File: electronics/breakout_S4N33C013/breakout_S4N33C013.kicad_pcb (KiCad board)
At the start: 4 copper layers, 2 parts

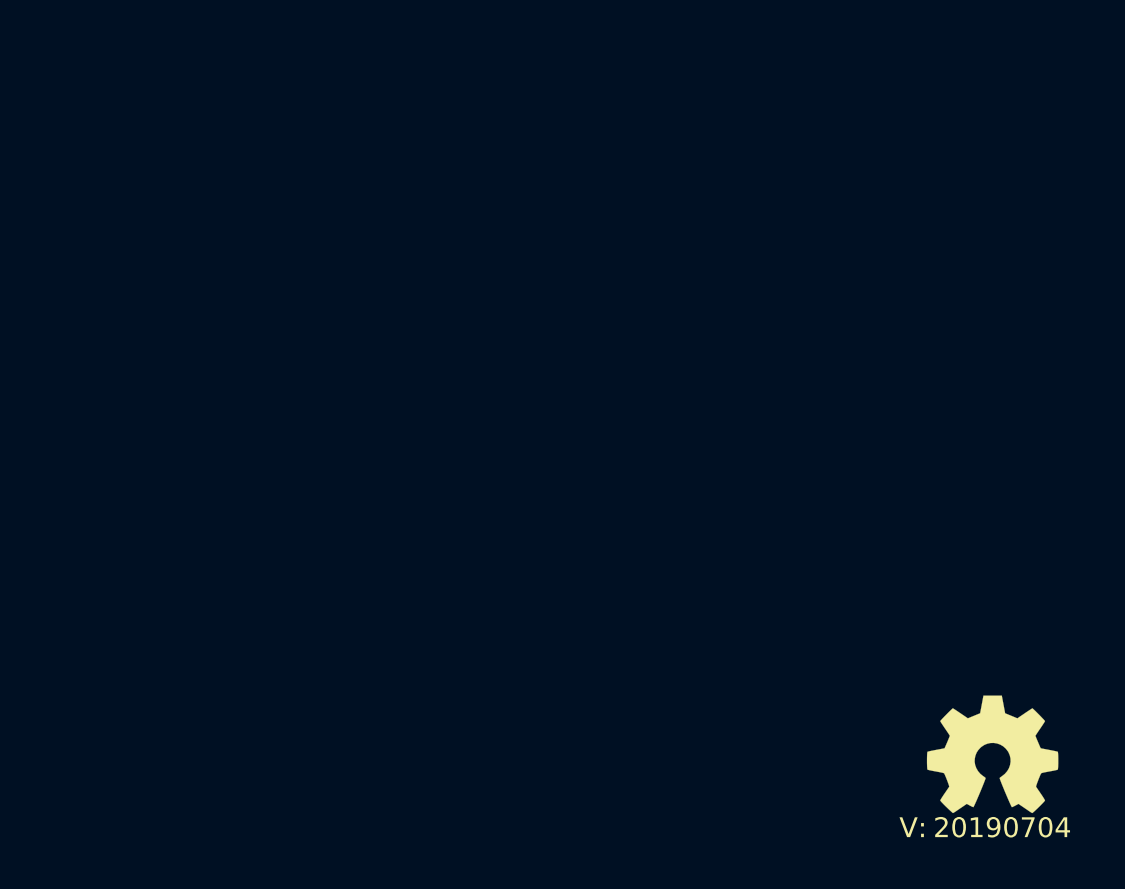
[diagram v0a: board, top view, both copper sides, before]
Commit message: Started initial layout for breakout
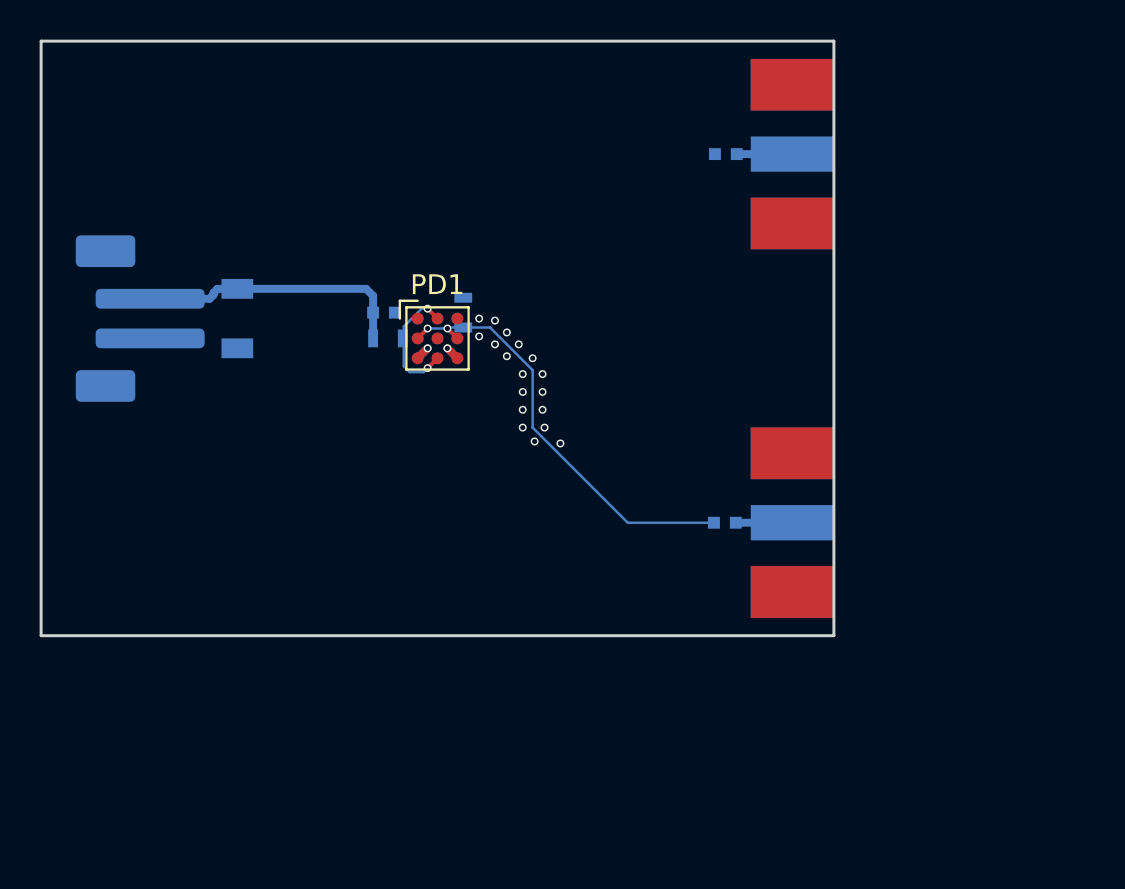
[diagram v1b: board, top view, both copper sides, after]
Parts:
- removed N1: OHWLOGO, Symbols:OSHW-Symbol_6.7x6mm_SilkScreen
- removed N2: 20190704, SquantorLabels:Label_version
- added C1: 100n, SquantorRcl:C_0402, B.Cu at (117.3, 78.7)
- added C2: 100n, SquantorRcl:C_0402, B.Cu at (134.5, 89.3)
- added C3: 100n, SquantorRcl:C_0402, B.Cu at (134.6, 70.7)
- added C4: 10u, SquantorRcl:C_1206, B.Cu at (109.9, 79.0)
- added J1: Conn_01x02, Connector_JST:JST_PH_B2B-PH-SM4-TB_1x02-1MP_P2.00mm_Vertical, B.Cu at (105.0, 79.0)
- added J2: Energy, SquantorConnectors:SMA_edge_6mm2, B.Cu at (137.9, 89.3)
- added J3: Timing, SquantorConnectors:SMA_edge_6mm2, B.Cu at (137.9, 70.7)
- added PD1: AFBR-S4N33C013, SquantorOpto:AFBR-S4N33C013, F.Cu at (120.0, 80.0)
- added R1: 50, SquantorRcl:R_0603, B.Cu at (121.3, 78.7)
- added R2: 50, SquantorRcl:R_0603, B.Cu at (117.5, 80.0)
- added TP1: PD_R, SquantorTestPoints:TestPoint_pad_circle_D05, B.Cu at (121.0, 81.0)
- added TP2: PD_R, SquantorTestPoints:TestPoint_pad_circle_D05, B.Cu at (119.0, 81.0)
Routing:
- net /PD_A: track 0.00 -> 21.7 mm, vias 0 -> 2
- net /VBIAS: track 0.00 -> 13.8 mm
- net /PD_C: track 0.00 -> 6.39 mm, vias 0 -> 2
- net Net-(C2-Pad1): track 0.00 -> 2.85 mm
- net Net-(C3-Pad1): track 0.00 -> 2.80 mm
- net Net-(PD1-Pad3C): track 0.00 -> 1.41 mm, vias 0 -> 1
- net Net-(PD1-Pad1C): track 0.00 -> 1.41 mm, vias 0 -> 1
- net /GND: vias 0 -> 18
- added copper zone on B.Cu, net /GND
- added copper zone on F.Cu, net /GND
- added copper zone on In1.Cu, net /GND
- added copper zone on In2.Cu, net /GND
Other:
- board outline added: 40 x 30 mm
- net class Default removed
